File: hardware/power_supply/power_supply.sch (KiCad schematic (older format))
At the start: 0 parts

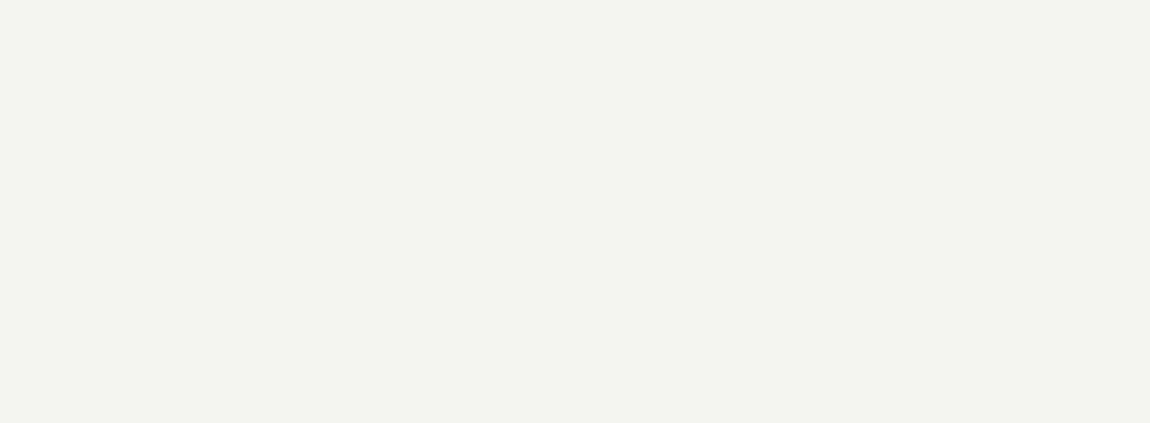
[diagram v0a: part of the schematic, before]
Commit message: Update: +5V regulator schematic
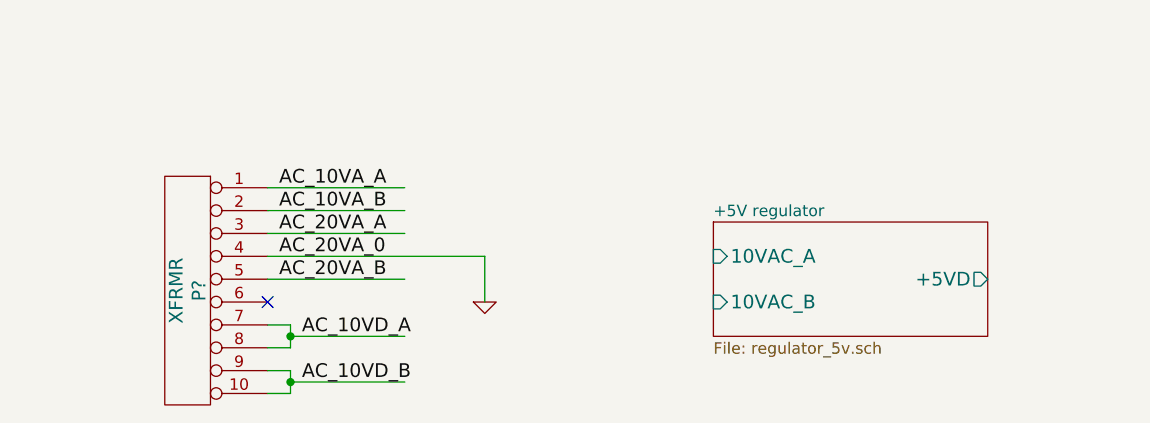
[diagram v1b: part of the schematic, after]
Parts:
- added P?: XFRMR, symbol CONN_10
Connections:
- net labels added: AC_10VA_A, AC_10VA_B, AC_10VD_A, AC_10VD_B, AC_20VA_0, AC_20VA_A, AC_20VA_B, GND
- wire segments 0 -> 16
- no-connect marks 0 -> 1
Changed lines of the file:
@@
 LIBS:contrib
 LIBS:valves
+LIBS:irlz44n
+LIBS:tl431
+LIBS:power_supply-cache
 EELAYER 24 0
 EELAYER END
 $Descr A4 11693 8268
 encoding utf-8
-Sheet 1 1
+Sheet 1 2
 Title "Loran C receiver power supply"
 Date "05 марта 2014"
@@
 Text Notes 650  2150 0    60   ~ 0
 Annotation:\nPower supply must provide following voltages:\n+5V digital supply\n+-15V analog supply\n+27V OCXO (oven-controlled crystal oscillator) supply\n\nMaximum continuous currents:\n+5V rail: 2.0A \n+-15V rails: 0.8A each\n+27V rail: 0.55A\n\nPrimary supply comes from mains, through a step-down transformer TPP289 (ТПП289) - generic USSR transformer model.\nNominal transformer power: 90W (90VA in some sources)\nTotal apparent power with maximum load: ~~105VA, so transformer would be slightly overloaded and needs proper ventilation.\n\nPermitted mains voltage variation: -15%/+5%, switchable primary windings allow even broader range.
+$Comp
+L CONN_10 P?
+U 1 1 5317B23A
+P 1500 3800
+F 0 "P?" V 1450 3800 60  0000 C CNN
+F 1 "XFRMR" V 1550 3800 60  0000 C CNN
+F 2 "" H 1500 3800 60  0000 C CNN
+F 3 "" H 1500 3800 60  0000 C CNN
+	1    1500 3800
+	-1   0    0    -1
+$EndComp
+Text Label 1900 3350 0    60   ~ 0
+AC_10VA_A
+Text Label 1900 3450 0    60   ~ 0
+AC_10VA_B
+Text Label 1900 3550 0    60   ~ 0
+AC_20VA_A
+Text Label 1900 3650 0    60   ~ 0
+AC_20VA_0
+Text Label 1900 3750 0    60   ~ 0
+AC_20VA_B
+Text Label 2000 4000 0    60   ~ 0
+AC_10VD_A
+Text Label 2000 4200 0    60   ~ 0
+AC_10VD_B
+NoConn ~ 1850 3850
+$Comp
+L GND #PWR?
+U 1 1 5317B345
+P 2800 3850
+F 0 "#PWR?" H 2800 3850 30  0001 C CNN
+F 1 "GND" H 2800 3780 30  0001 C CNN
+F 2 "" H 2800 3850 60  0000 C CNN
+F 3 "" H 2800 3850 60  0000 C CNN
+	1    2800 3850
+	1    0    0    -1
+$EndComp
+Wire Wire Line
+	1850 4050 1950 4050
+Wire Wire Line
+	1950 4050 1950 4000
+Wire Wire Line
+	1950 4000 1950 3950
+Wire Wire Line
+	1950 3950 1850 3950
+Wire Wire Line
+	1850 4150 1950 4150
+Wire Wire Line
+	1950 4150 1950 4200
+Wire Wire Line
+	1950 4200 1950 4250
+Wire Wire Line
+	1950 4250 1850 4250
+Wire Wire Line
+	1950 4200 2450 4200
+Connection ~ 1950 4200
+Wire Wire Line
+	1950 4000 2450 4000
+Connection ~ 1950 4000
+Wire Wire Line
+	1850 3750 2450 3750
+Wire Wire Line
+	1850 3650 2800 3650
+Wire Wire Line
+	1850 3550 2450 3550
+Wire Wire Line
+	1850 3450 2450 3450
+Wire Wire Line
+	1850 3350 2450 3350
+Wire Wire Line
+	2800 3650 2800 3850
+$Sheet
+S 3800 3500 1200 500
+U 5317B73E
+F0 "+5V regulator" 50
+F1 "regulator_5v.sch" 50
+F2 "10VAC_A" I L 3800 3650 60
+F3 "10VAC_B" I L 3800 3850 60
+F4 "+5VD" O R 5000 3750 60
+$EndSheet
 $EndSCHEMATC

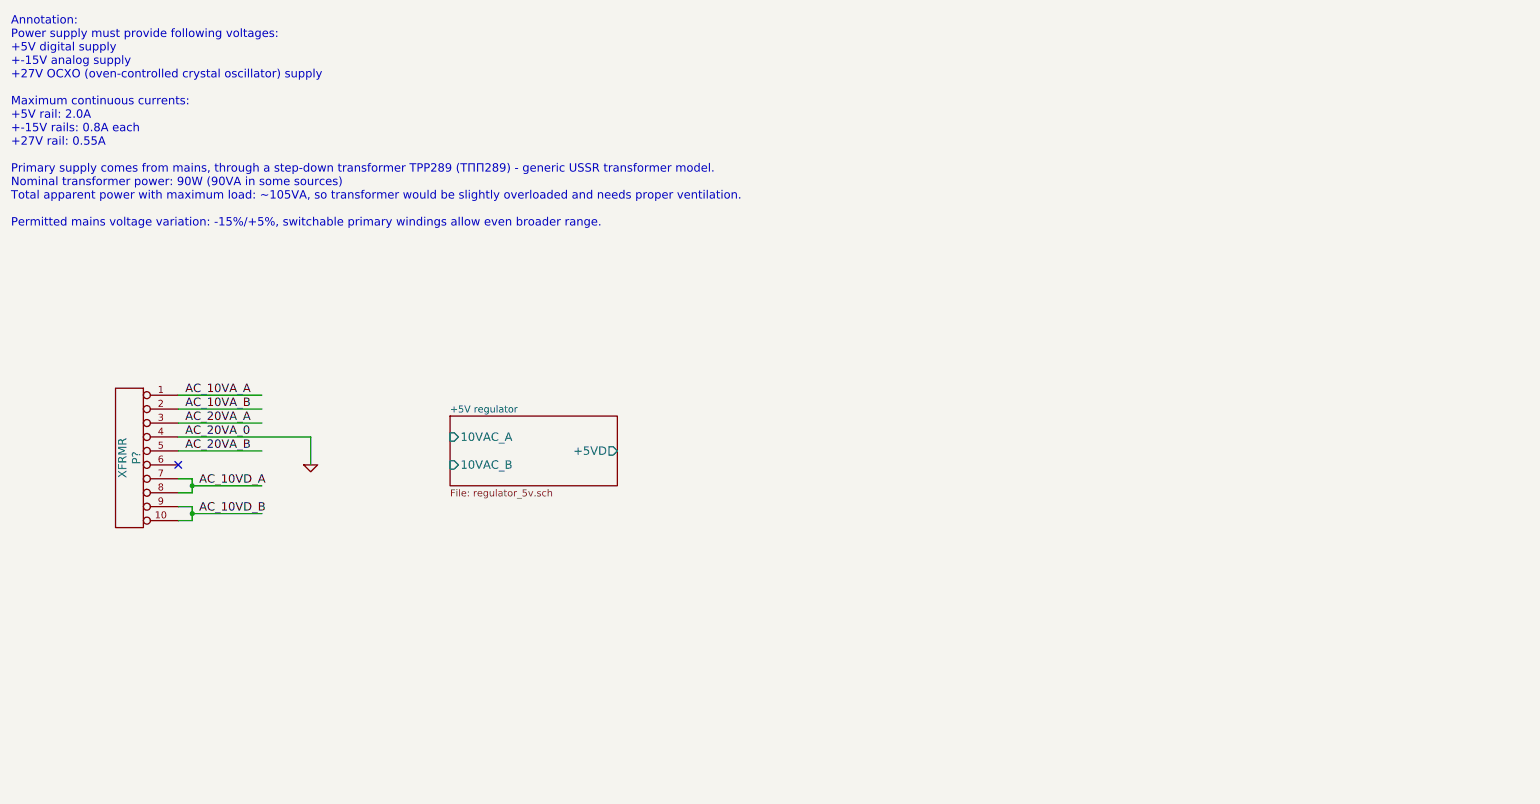
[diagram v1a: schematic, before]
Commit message: Update: +-15V regulator schematic almost complete
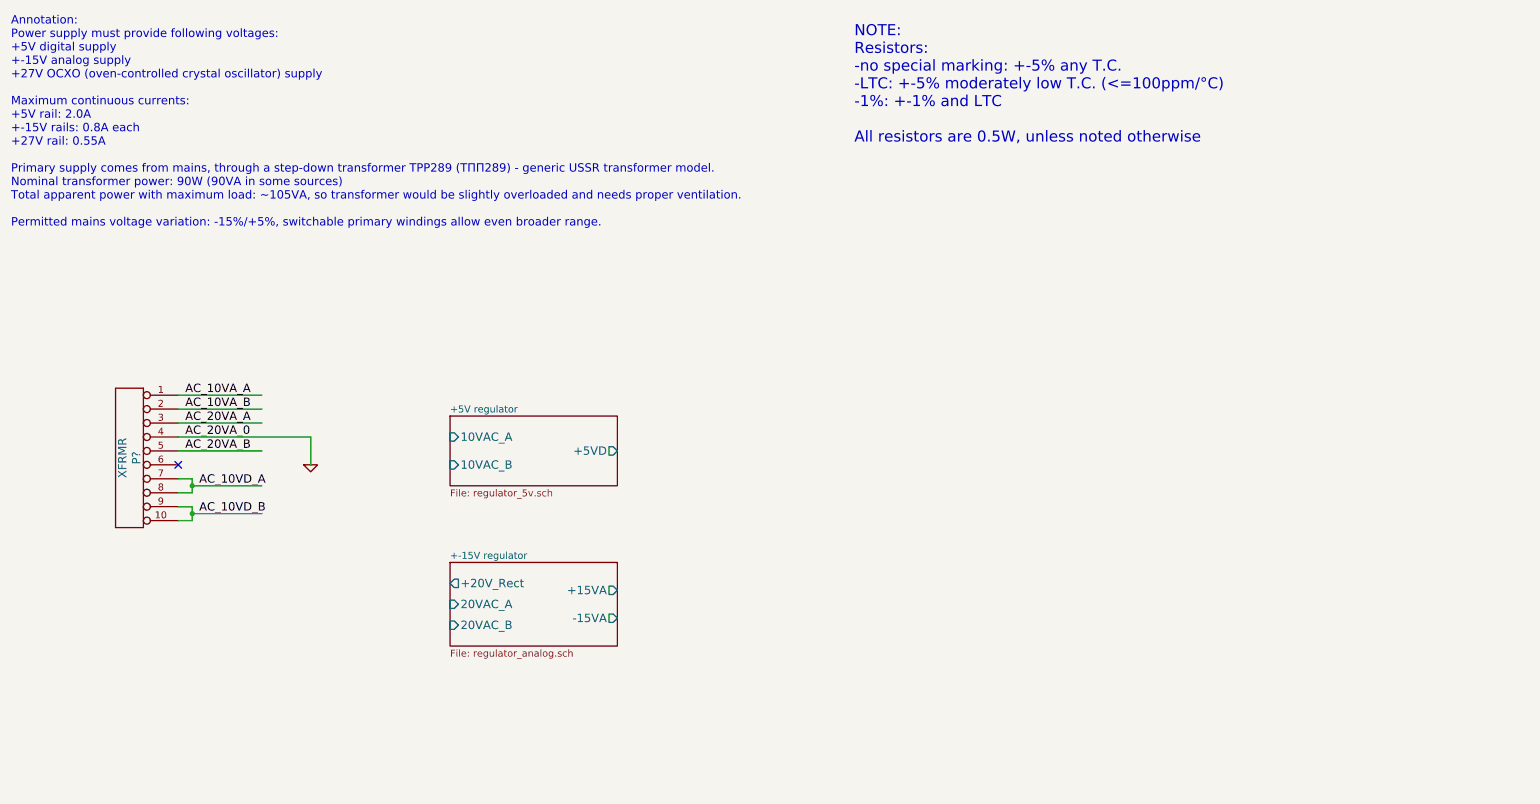
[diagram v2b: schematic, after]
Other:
- note added: "NOTE:\nResistors:\n-no special marking: +-5% any T.C.\n-LTC: +-5% moderately low T.C. (<=100ppm/°C)\n-1%: +-1% and LTC\n\nAll resistors are 0.5W, unless noted otherwise"
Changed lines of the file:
@@
 LIBS:irlz44n
 LIBS:tl431
+LIBS:r_pot
 LIBS:power_supply-cache
 EELAYER 24 0
@@
 $Descr A4 11693 8268
 encoding utf-8
-Sheet 1 2
+Sheet 1 3
 Title "Loran C receiver power supply"
 Date "05 марта 2014"
@@
 F4 "+5VD" O R 5000 3750 60
 $EndSheet
+$Sheet
+S 3800 4550 1200 600
+U 5322E404
+F0 "+-15V regulator" 50
+F1 "regulator_analog.sch" 50
+F2 "20VAC_A" I L 3800 4850 60
+F3 "20VAC_B" I L 3800 5000 60
+F4 "+20V_Rect" O L 3800 4700 60
+F5 "+15VA" O R 5000 4750 60
+F6 "-15VA" O R 5000 4950 60
+$EndSheet
+Text Notes 6700 1550 0    79   ~ 0
+NOTE:\nResistors:\n-no special marking: +-5% any T.C.\n-LTC: +-5% moderately low T.C. (<=100ppm/°C)\n-1%: +-1% and LTC\n\nAll resistors are 0.5W, unless noted otherwise
 $EndSCHEMATC

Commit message: Update: almost finished power supply schematic (incl. +24V)
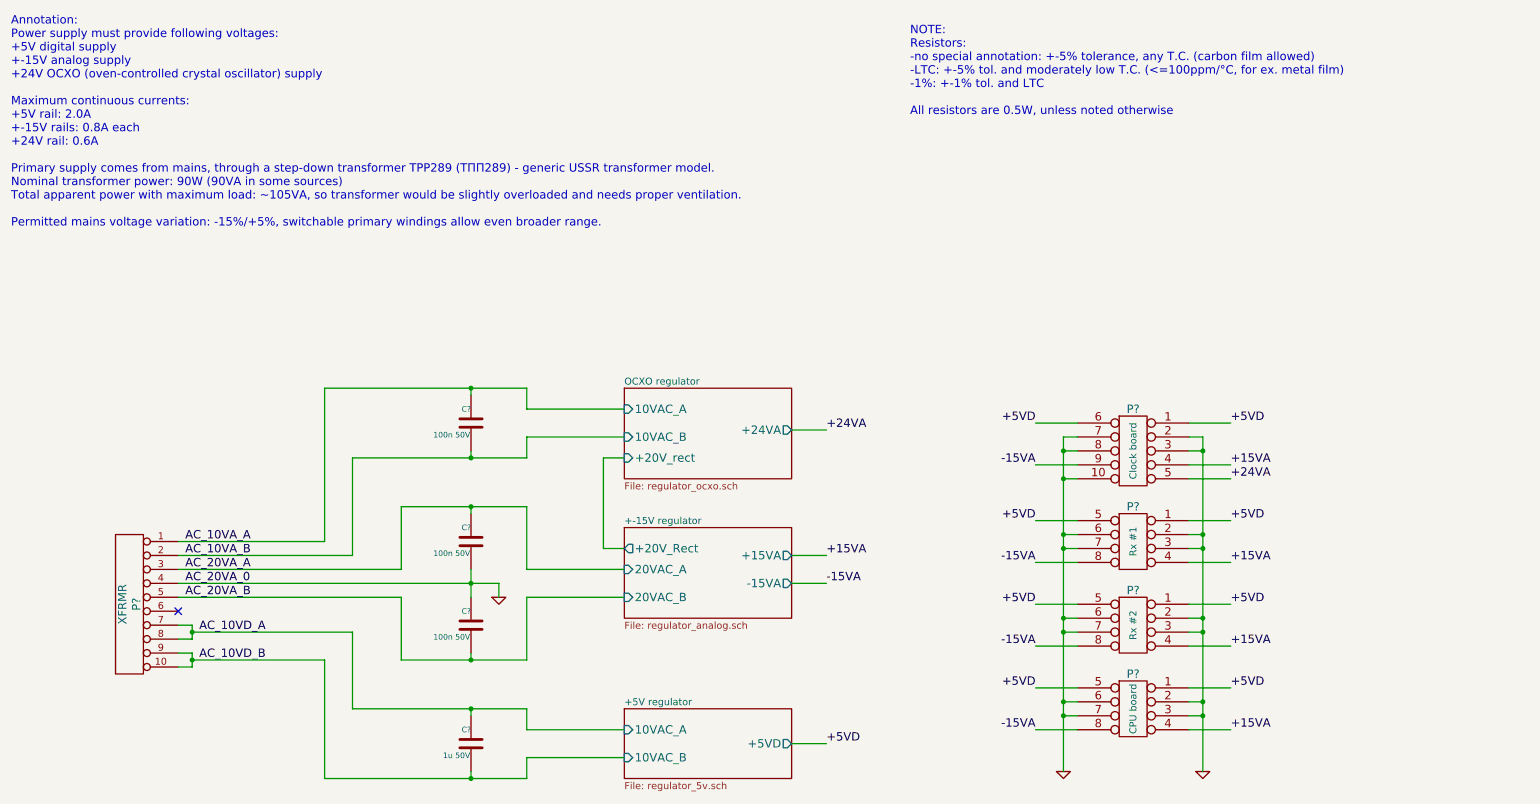
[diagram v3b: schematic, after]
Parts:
- added C?: 1u 50V, symbol C
- added C? (x3): 100n 50V, symbol C
- added P?: CPU board, symbol MF_8
- added P?: Clock board, symbol MF_10
- added P?: Rx #2, symbol MF_8
- added P?: Rx #1, symbol MF_8
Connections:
- net labels added: +15VA, +24VA, +5VD, -15VA
- wire segments 16 -> 113
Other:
- note added: "Annotation:\nPower supply must provide following voltages:\n+5V digital supply\n+-15V analog supply\n+24V OCXO (oven-controlled crystal oscillator) supply\n\nMaximum continuous currents:\n+5V rail: 2.0A \n+-15V rails: 0.8A each\n+24V rail: 0.6A\n\nPrimary supply comes from mains, through a step-down transformer TPP289 (ТПП289) - generic USSR transformer model.\nNominal transformer power: 90W (90V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"
- note added: "NOTE:\nResistors:\n-no special annotation: +-5% tolerance, any T.C. (carbon film allowed)\n-LTC: +-5% tol. and moderately low T.C. (<=100ppm/°C, for ex. metal film)\n-1%: +-1% tol. and LTC\n\nAll resistors are 0.5W, unless noted otherwise"
- note removed: "Annotation:\nPower supply must provide following voltages:\n+5V digital supply\n+-15V analog supply\n+27V OCXO (oven-controlled crystal oscillator) supply\n\nMaximum continuous currents:\n+5V rail: 2.0A \n+-15V rails: 0.8A each\n+27V rail: 0.55A\n\nPrimary supply comes from mains, through a step-down transformer TPP289 (ТПП289) - generic USSR transformer model.\nNominal transformer power: 90W (90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"
- note removed: "NOTE:\nResistors:\n-no special marking: +-5% any T.C.\n-LTC: +-5% moderately low T.C. (<=100ppm/°C)\n-1%: +-1% and LTC\n\nAll resistors are 0.5W, unless noted otherwise"
- moved on the sheet: P?
